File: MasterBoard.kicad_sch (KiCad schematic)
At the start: 0 parts

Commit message: Внутренние изменения
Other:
- added sheet SD-card (schematics/SPI_micro_SD.kicad_sch)
- added sheet USART_module (schematics/USART_module.kicad_sch)
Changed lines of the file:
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@@
+	(wire
+		(pts
+			(xy 40.64 46.99) (xy 58.42 46.99)
+		)
+		(stroke
+			(width 0)
+			(type default)
+		)
+	)
 	(wire
 		(pts
@@
 	(wire
 		(pts
+			(xy 40.64 34.29) (xy 58.42 34.29)
+		)
+		(stroke
+			(width 0)
+			(type default)
+		)
+	)
+	(wire
+		(pts
 			(xy 177.8 38.1) (xy 195.58 38.1)
 		)
@@
 	(wire
 		(pts
+			(xy 40.64 52.07) (xy 58.42 52.07)
+		)
+		(stroke
+			(width 0)
+			(type default)
+		)
+	)
+	(wire
+		(pts
 			(xy 109.22 55.88) (xy 127 55.88)
 		)
@@
 	(wire
 		(pts
+			(xy 40.64 49.53) (xy 58.42 49.53)
+		)
+		(stroke
+			(width 0)
+			(type default)
+		)
+	)
+	(wire
+		(pts
 			(xy 177.8 114.3) (xy 195.58 114.3)
 		)
@@
 		(pts
 			(xy 109.22 30.48) (xy 127 30.48)
+		)
+		(stroke
+			(width 0)
+			(type default)
+		)
+	)
+	(wire
+		(pts
+			(xy 40.64 54.61) (xy 58.42 54.61)
+		)
+		(stroke
+			(width 0)
+			(type default)
+		)
+	)
+	(wire
+		(pts
+			(xy 40.64 31.75) (xy 58.42 31.75)
 		)
 		(stroke
@@
 	)
 	(sheet
+		(at 25.4 29.21)
+		(size 15.24 11.176)
+		(exclude_from_sim no)
+		(in_bom yes)
+		(on_board yes)
+		(dnp no)
+		(fields_autoplaced yes)
+		(stroke
+			(width 0.1524)
+			(type solid)
+		)
+		(fill
+			(color 255 255 194 1.0000)
+		)
+		(property "Sheetname" "USART_module"
+			(at 25.4 28.4984 0)
+			(effects
+				(font
+					(size 1.27 1.27)
+				)
+				(justify left bottom)
+			)
+		)
+		(property "Sheetfile" "schematics/USART_module.kicad_sch"
+			(at 25.4 40.9706 0)
+			(effects
+				(font
+					(size 1.27 1.27)
+				)
+				(justify left top)
+				(hide yes)
+			)
+		)
+		(pin "RX" input
+			(at 40.64 34.29 0)
+			(effects
+				(font
+					(size 1.27 1.27)
+				)
+				(justify right)
+			)
+		)
+		(pin "TX" output
+			(at 40.64 31.75 0)
+			(effects
+				(font
+					(size 1.27 1.27)
+				)
+				(justify right)
+			)
+		)
+		(instances
+			(project "MasterBoard"
+				(path "/97e8f341-b455-4614-ab7f-cc310164e7aa"
+					(page "5")
+				)
+			)
+		)
+	)
+	(sheet
 		(at 45.72 172.72)
 		(size 38.1 13.97)
@@
 				)
 			)
+		)
+	)
+	(sheet
+		(at 25.4 44.45)
+		(size 15.24 13.97)
+		(exclude_from_sim no)
+		(in_bom yes)
+		(on_board yes)
+		(dnp no)
+		(fields_autoplaced yes)
+		(stroke
+			(width 0.1524)
+			(type solid)
+		)
+		(fill
+			(color 255 255 194 1.0000)
+		)
+		(property "Sheetname" "SD-card"
+			(at 25.4 43.7384 0)
+			(effects
+				(font
+					(size 1.27 1.27)
+				)
+				(justify left bottom)
+			)
+		)
+		(property "Sheetfile" "schematics/SPI_micro_SD.kicad_sch"
+			(at 25.4 59.0046 0)
+			(effects
+				(font
+					(size 1.27 1.27)
+				)
+				(justify left top)
+				(hide yes)
+			)
+		)
+		(pin "SPI_CS" bidirectional
+			(at 40.64 46.99 0)
+			(effects
+				(font
+					(size 1.27 1.27)
+				)
+				(justify right)
+			)
+		)
+		(pin "SPI_MISO" bidirectional
+			(at 40.64 49.53 0)
+			(effects
+				(font
+					(size 1.27 1.27)
+				)
+				(justify right)
+			)
+		)
+		(pin "SPI_MOSI" bidirectional
+			(at 40.64 52.07 0)
+			(effects
+				(font
+					(size 1.27 1.27)
+				)
+				(justify right)
+			)
+		)
+		(pin "SPI_SCK" bidirectional
+			(at 40.64 54.61 0)
+			(effects
+				(font
+					(size 1.27 1.27)
+				)
+				(justify right)
+			)
+		)
+		(instances
+			(project "MasterBoard"
+				(path "/97e8f341-b455-4614-ab7f-cc310164e7aa"
+					(page "6")
+				)
+			)

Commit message: Добавил много схем, близок к тому чтобы общий вид платы доделать
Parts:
- added J6: IDC-16, Connector_IDC:IDC-Header_2x08_P2.54mm_Horizontal, symbol Connector_Generic:Conn_02x08_Top_Bottom
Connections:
- new net +12V: J6.7 (Pin_7), J6.9 (Pin_9)
- new net +24V: J6.11 (Pin_11), J6.13 (Pin_13), J6.15 (Pin_15)
- new net +5V: J6.5 (Pin_5)
- new net BOOT0: J6.1 (Pin_1)
- new net GND: J6.10 (Pin_10), J6.12 (Pin_12), J6.14 (Pin_14), J6.16 (Pin_16), J6.6 (Pin_6), J6.8 (Pin_8)
- new net NRST: J6.2 (Pin_2)
- new net USART_RX: J6.4 (Pin_4)
- new net USART_TX: J6.3 (Pin_3)
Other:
- added sheet Motor (schematics/Motor.kicad_sch)
- added sheet TMP102 (schematics/TMP102.kicad_sch)
- added sheet Table (schematics/Table.kicad_sch)

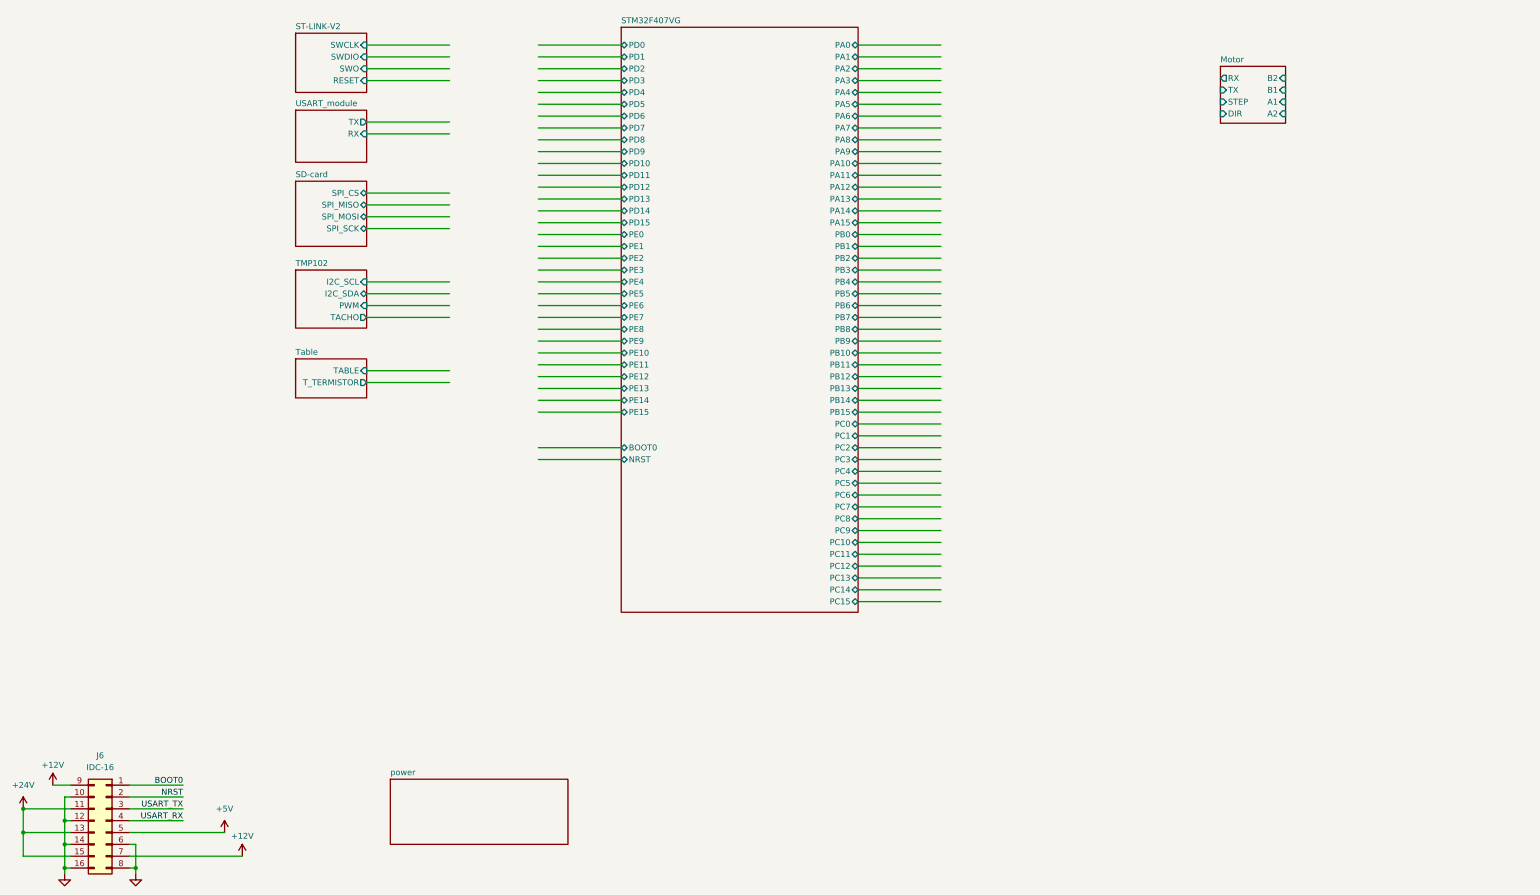
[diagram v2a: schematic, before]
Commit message: Добавил движки, концевики, и шлейфы
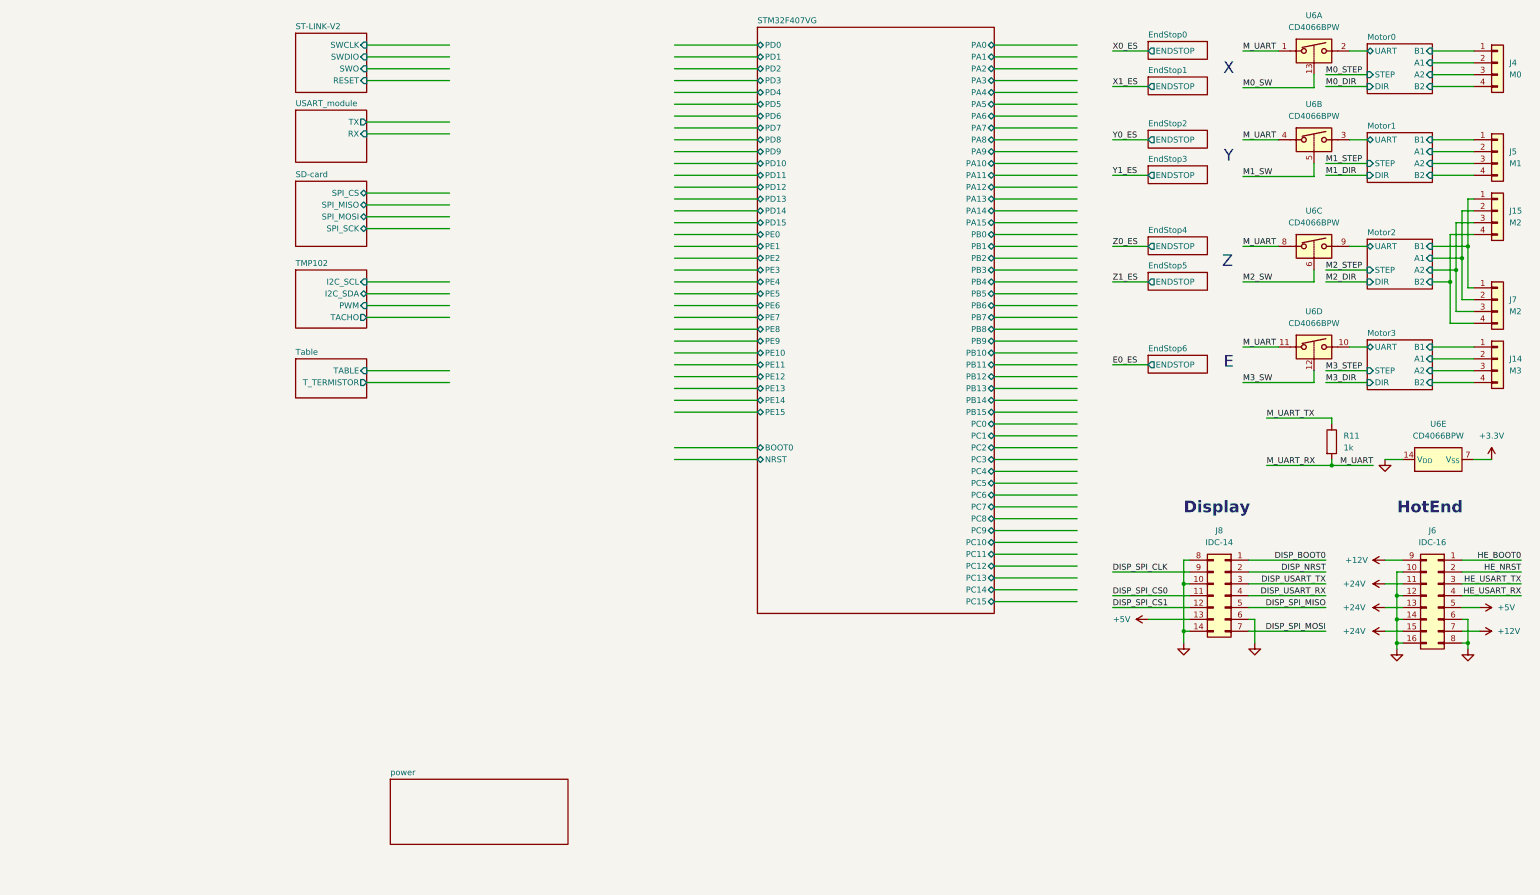
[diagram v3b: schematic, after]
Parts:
- added J14: M3, symbol Connector_Generic:Conn_01x04
- added J15, J7: M2, symbol Connector_Generic:Conn_01x04
- added J4: M0, symbol Connector_Generic:Conn_01x04
- added J5: M1, symbol Connector_Generic:Conn_01x04
- added J8: IDC-14, Connector_IDC:IDC-Header_2x07_P2.54mm_Vertical, symbol Connector_Generic:Conn_02x07_Top_Bottom
- added R11: 1k, symbol Device:R
- added U6: CD4066BPW, Package_SO:TSSOP-14_4.4x5mm_P0.65mm, symbol Analog_Switch:CD4066BPW
- J6: footprint Connector_IDC:IDC-Header_2x08_P2.54mm_Horizontal -> Connector_IDC:IDC-Header_2x08_P2.54mm_Vertical
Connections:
- net +5V: now also J8.13 (Pin_13)
- net GND: now also J8.10 (Pin_10), J8.14 (Pin_14), J8.6 (Pin_6), J8.8 (Pin_8), U6.14 (V_{DD})
- net Motor0/A1: now also J4.2 (Pin_2)
- net Motor0/A2: now also J4.3 (Pin_3)
- net Motor0/B1: now also J4.1 (Pin_1)
- net Motor0/B2: now also J4.4 (Pin_4)
- net BOOT0 renamed HE_BOOT0
- net NRST renamed HE_NRST
- net USART_RX renamed HE_USART_RX
- net USART_TX renamed HE_USART_TX
- new net +3.3V: U6.7 (V_{SS})
- new net DISP_BOOT0: J8.1 (Pin_1)
- new net DISP_NRST: J8.2 (Pin_2)
- new net DISP_SPI_CLK: J8.9 (Pin_9)
- new net DISP_SPI_CS0: J8.11 (Pin_11)
- new net DISP_SPI_CS1: J8.12 (Pin_12)
- new net DISP_SPI_MISO: J8.5 (Pin_5)
- new net DISP_SPI_MOSI: J8.7 (Pin_7)
- new net DISP_USART_RX: J8.4 (Pin_4)
- new net DISP_USART_TX: J8.3 (Pin_3)
- new net M0_SW: U6.13
- new net M1_SW: U6.5
- new net M2_SW: U6.6
- new net M3_SW: U6.12
- new net M_UART: R11.2, U6.1, U6.11, U6.4, U6.8
- new net M_UART_TX: R11.1
- new net Motor0/UART: U6.2
- new net Motor1/A1: J5.2 (Pin_2)
- new net Motor1/A2: J5.3 (Pin_3)
- new net Motor1/B1: J5.1 (Pin_1)
- new net Motor1/B2: J5.4 (Pin_4)
- new net Motor1/UART: U6.3
- new net Motor2/A1: J15.2 (Pin_2), J7.2 (Pin_2)
- new net Motor2/A2: J15.3 (Pin_3), J7.3 (Pin_3)
- new net Motor2/B1: J15.1 (Pin_1), J7.1 (Pin_1)
- new net Motor2/B2: J15.4 (Pin_4), J7.4 (Pin_4)
- new net Motor2/UART: U6.9
- new net Motor3/A1: J14.2 (Pin_2)
- new net Motor3/A2: J14.3 (Pin_3)
- new net Motor3/B1: J14.1 (Pin_1)
- new net Motor3/B2: J14.4 (Pin_4)
- new net Motor3/UART: U6.10
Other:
- sheet Motor renamed Motor0
- added sheet EndStop0 (schematics/EndStop.kicad_sch)
- added sheet EndStop1 (schematics/EndStop.kicad_sch)
- added sheet EndStop2 (schematics/EndStop.kicad_sch)
- added sheet EndStop3 (schematics/EndStop.kicad_sch)
- added sheet EndStop4 (schematics/EndStop.kicad_sch)
- added sheet EndStop5 (schematics/EndStop.kicad_sch)
- added sheet EndStop6 (schematics/EndStop.kicad_sch)
- added sheet Motor1 (schematics/Motor.kicad_sch)
- added sheet Motor2 (schematics/Motor.kicad_sch)
- added sheet Motor3 (schematics/Motor.kicad_sch)
- sheet Motor0 ports: added UART; removed RX, TX
- note added: "Display"
- note added: "E"
- note added: "HotEnd"
- note added: "X"
- note added: "Y"
- note added: "Z"
- moved on the sheet: J6

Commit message: Добавил модуль W5500. Посчитал амбиции платы, не хватает пинов в МК, решил удалить(убрать из симуляции) концевики дополнительные
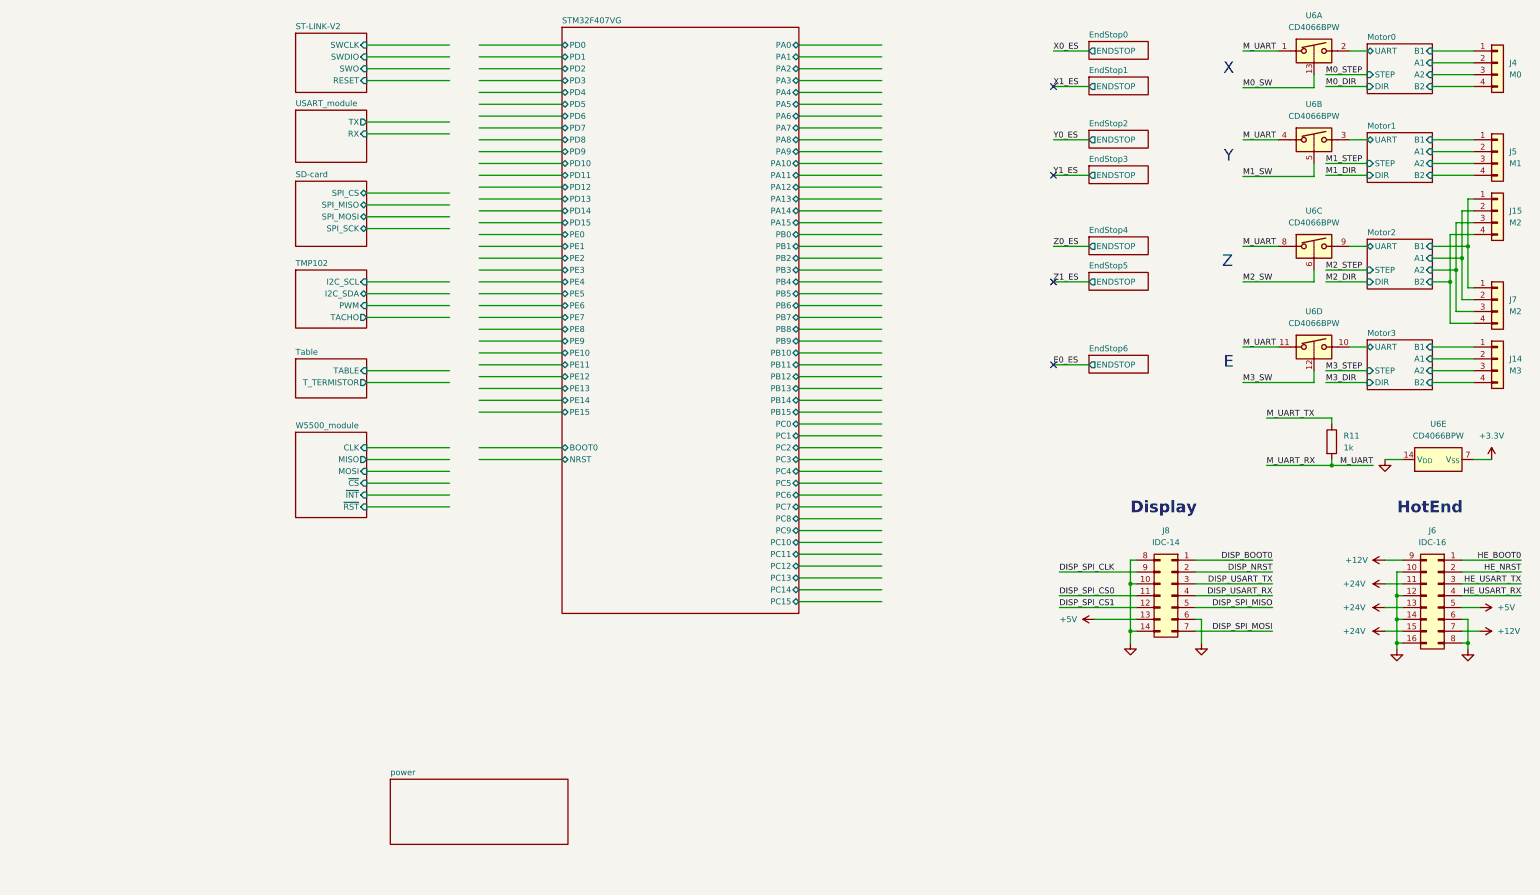
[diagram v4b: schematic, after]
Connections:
- no-connect marks 0 -> 4
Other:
- added sheet W5500_module (schematics/W5500_module.kicad_sch)
- moved on the sheet: J8

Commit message: Начал править нумерацию элементов, и устанавливать посадочные места
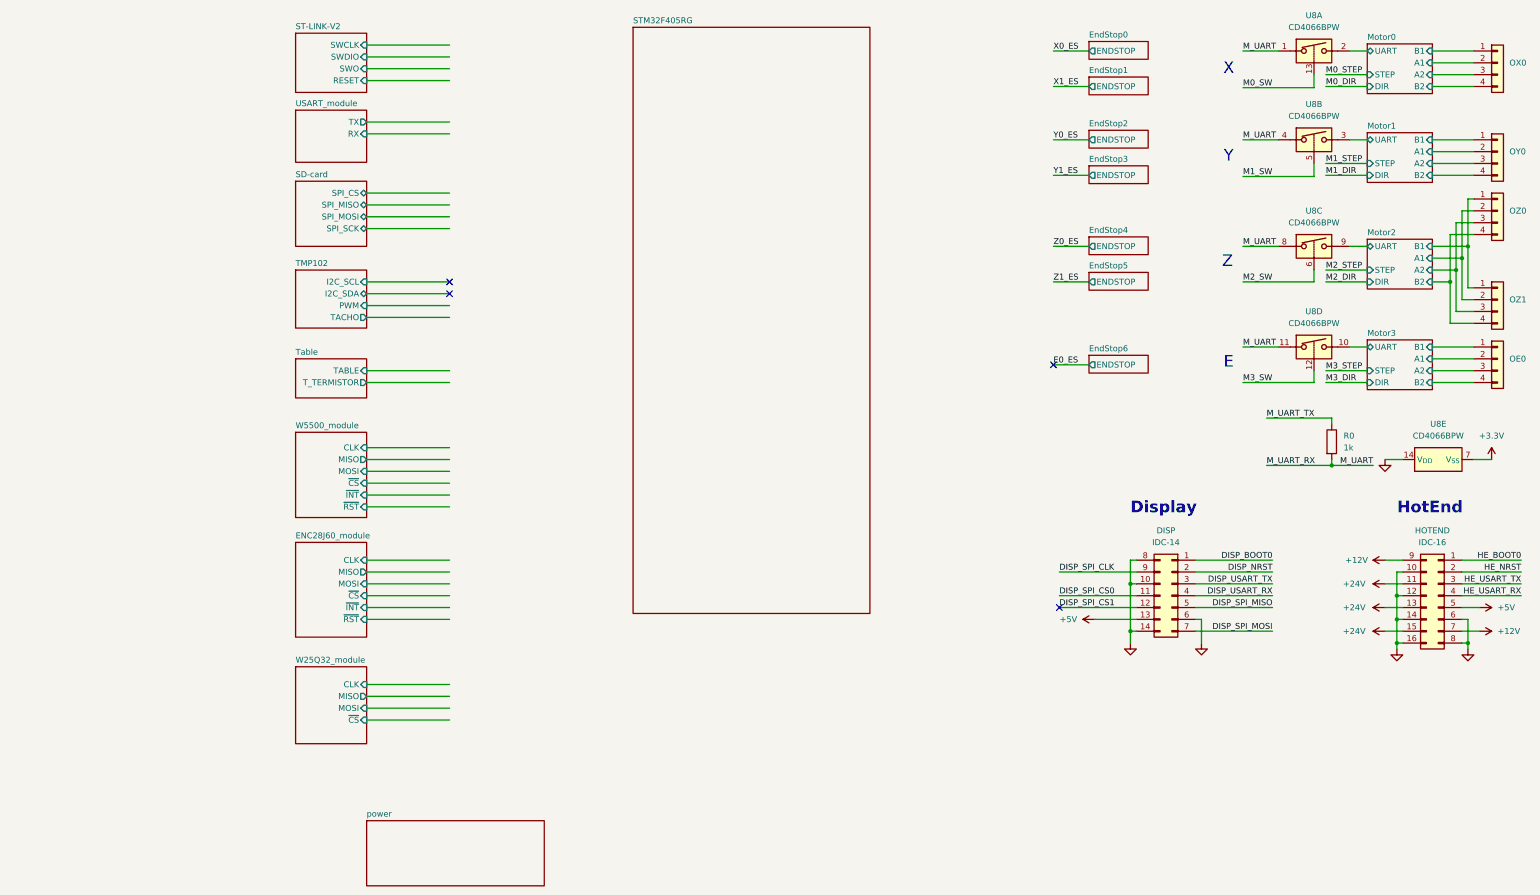
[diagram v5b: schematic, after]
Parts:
- renumbered J8 to DISP, J6 to HOTEND, J14 to OE0, J4 to OX0, J5 to OY0, J15 to OZ0, J7 to OZ1, R11 to R0, U6 to U8
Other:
- sheet STM32F407VG renamed STM32F405RG
- added sheet ENC28J60_module (schematics/ENC28J60_module.kicad_sch)
- added sheet W25Q32_module (schematics/W25Q32_module.kicad_sch)
- sheet STM32F405RG: file schematics/stm32f407vg.kicad_sch -> schematics/STM32f405RG.kicad_sch
- sheet STM32F405RG ports: added none; removed BOOT0, NRST, PA0, PA1, PA10, PA11, PA12, PA13, PA14, PA15, PA2, PA3, PA4, PA5, PA6, PA7, PA8, PA9, PB0, PB1, PB10, PB11, PB12, PB13, PB14, PB15, PB2, PB3, PB4, PB5, PB6, PB7, PB8, PB9, PC0, PC1, PC10, PC11, PC12, PC13, PC14, PC15, PC2, PC3, PC4, PC5, PC6, PC7, PC8, PC9, PD0, PD1, PD10, PD11, PD12, PD13, PD14, PD15, PD2, PD3, PD4, PD5, PD6, PD7, PD8, PD9, PE0, PE1, PE10, PE11, PE12, PE13, PE14, PE15, PE2, PE3, PE4, PE5, PE6, PE7, PE8, PE9

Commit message: Часть с схемой платы в кокойто степени дошла до этапа дебага
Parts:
- OE0, OX0, OY0, OZ0, OZ1: footprint (none) -> Connector_JST:JST_XH_B4B-XH-A_1x04_P2.50mm_Vertical
- R9800: renamed from R0; footprint (none) -> Resistor_SMD:R_0805_2012Metric
- renumbered DISP to DISP0, HOTEND to HOTEND0
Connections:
- net Motor0/A1: now also OX0.3 (Pin_3); no longer OX0.2 (Pin_2)
- net Motor0/A2: now also OX0.4 (Pin_4); no longer OX0.3 (Pin_3)
- net Motor0/B1: now also OX0.2 (Pin_2); no longer OX0.1 (Pin_1)
- net Motor0/B2: now also OX0.1 (Pin_1); no longer OX0.4 (Pin_4)
- net Motor1/A1: now also OY0.3 (Pin_3); no longer OY0.2 (Pin_2)
- net Motor1/A2: now also OY0.4 (Pin_4); no longer OY0.3 (Pin_3)
- net Motor1/B1: now also OY0.2 (Pin_2); no longer OY0.1 (Pin_1)
- net Motor1/B2: now also OY0.1 (Pin_1); no longer OY0.4 (Pin_4)
- net Motor2/A1: now also OZ0.3 (Pin_3), OZ1.3 (Pin_3); no longer OZ0.2 (Pin_2), OZ1.2 (Pin_2)
- net Motor2/A2: now also OZ0.4 (Pin_4), OZ1.4 (Pin_4); no longer OZ0.3 (Pin_3), OZ1.3 (Pin_3)
- net Motor2/B1: now also OZ0.2 (Pin_2), OZ1.2 (Pin_2); no longer OZ0.1 (Pin_1), OZ1.1 (Pin_1)
- net Motor2/B2: now also OZ0.1 (Pin_1), OZ1.1 (Pin_1); no longer OZ0.4 (Pin_4), OZ1.4 (Pin_4)
- net Motor3/A1: now also OE0.3 (Pin_3); no longer OE0.2 (Pin_2)
- net Motor3/A2: now also OE0.4 (Pin_4); no longer OE0.3 (Pin_3)
- net Motor3/B1: now also OE0.2 (Pin_2); no longer OE0.1 (Pin_1)
- net Motor3/B2: now also OE0.1 (Pin_1); no longer OE0.4 (Pin_4)
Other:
- sheet STM32F405RG ports: added NRST, PA0, PA1, PA10, PA11, PA12, PA13, PA14, PA15, PA2, PA3, PA4, PA5, PA6, PA7, PA8, PA9, PB0, PB1, PB10, PB11, PB12, PB13, PB14, PB15, PB2, PB3, PB4, PB5, PB6, PB7, PB8, PB9, PC0, PC1, PC10, PC11, PC12, PC13, PC14, PC15, PC2, PC3, PC4, PC5, PC6, PC7, PC8, PC9, PD2; removed none
- company: (none) -> Филимонов и К
